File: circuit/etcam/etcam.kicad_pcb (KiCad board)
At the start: 2 copper layers, 100 x 50 mm, 86 parts, among them J1 SWD_connector, J2 USB_connector, J3 ESC_signal_connector, J4 ESC_GND_connector, J5 MCU_PWR_SRC_selector, J6 jumper_park, SW1 reset_SW, U1 FT232RL, U2 Si8640BB-B-IS1, U3 Si8640BB-B-IS1, U4 Si8640BB-B-IS1, U5 Si8640BB-B-IS1, U6 74HC251, U7 STM32F303xD/E-LQFP64, U8 LM1117-3.3, U9 ADuM5020, Y1 8MHz

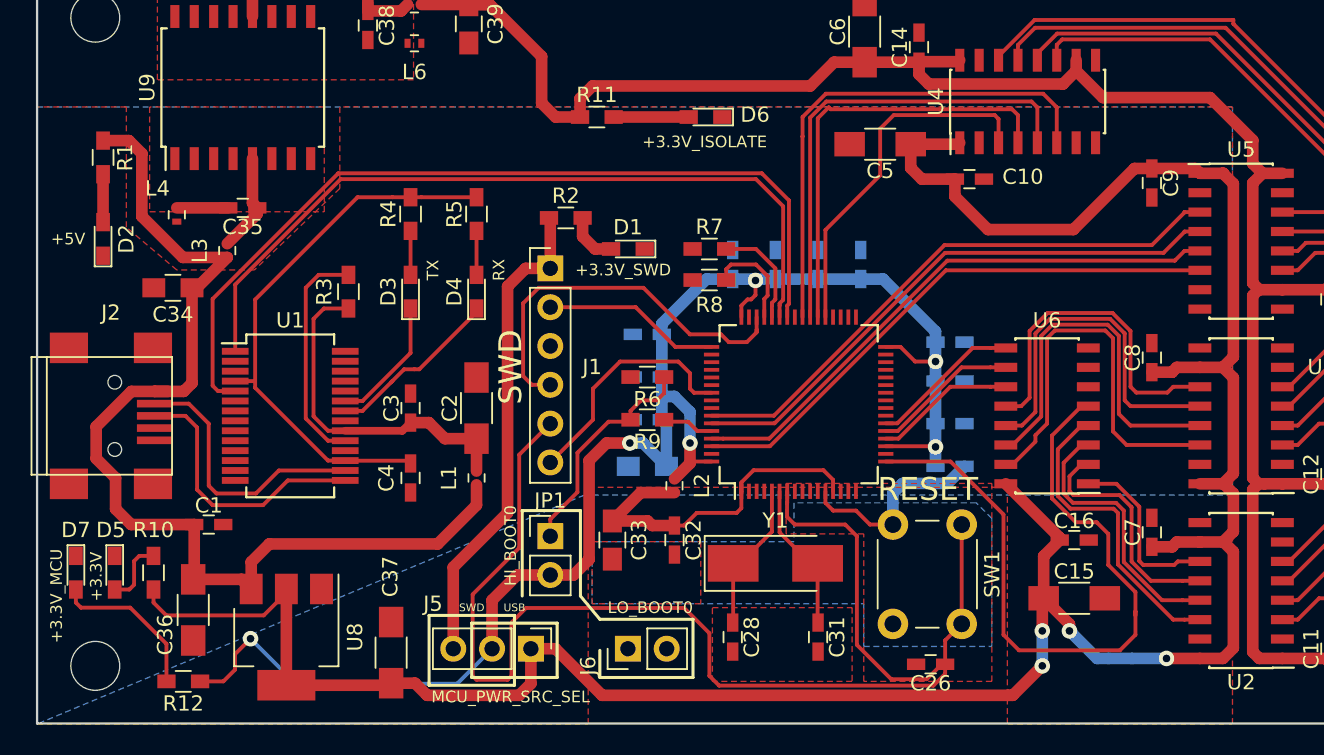
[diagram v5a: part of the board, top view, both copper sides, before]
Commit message: added via between front and back GND plane in ETCAM PCB
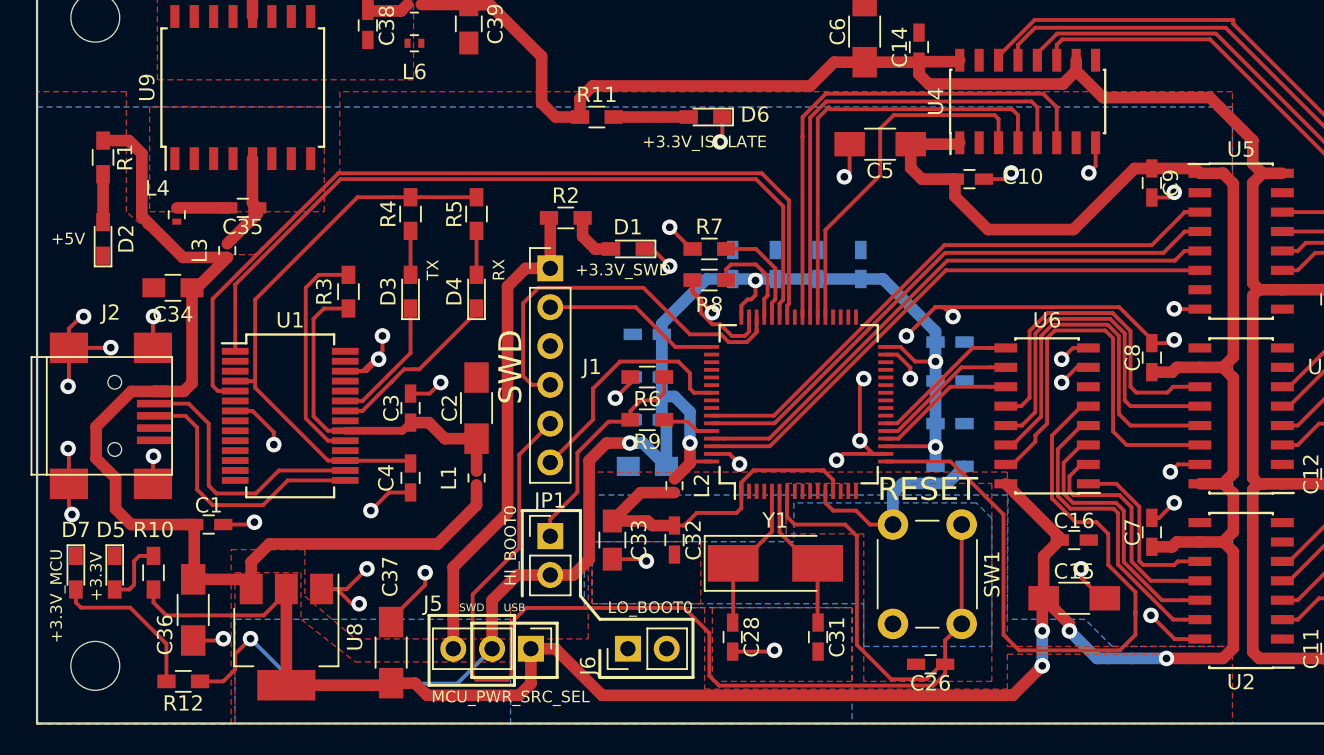
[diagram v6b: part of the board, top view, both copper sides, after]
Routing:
- net GND: track 13.2 -> 142.1 mm, vias 0 -> 43
- added copper zone on F.Cu, net /+3.3V_USB

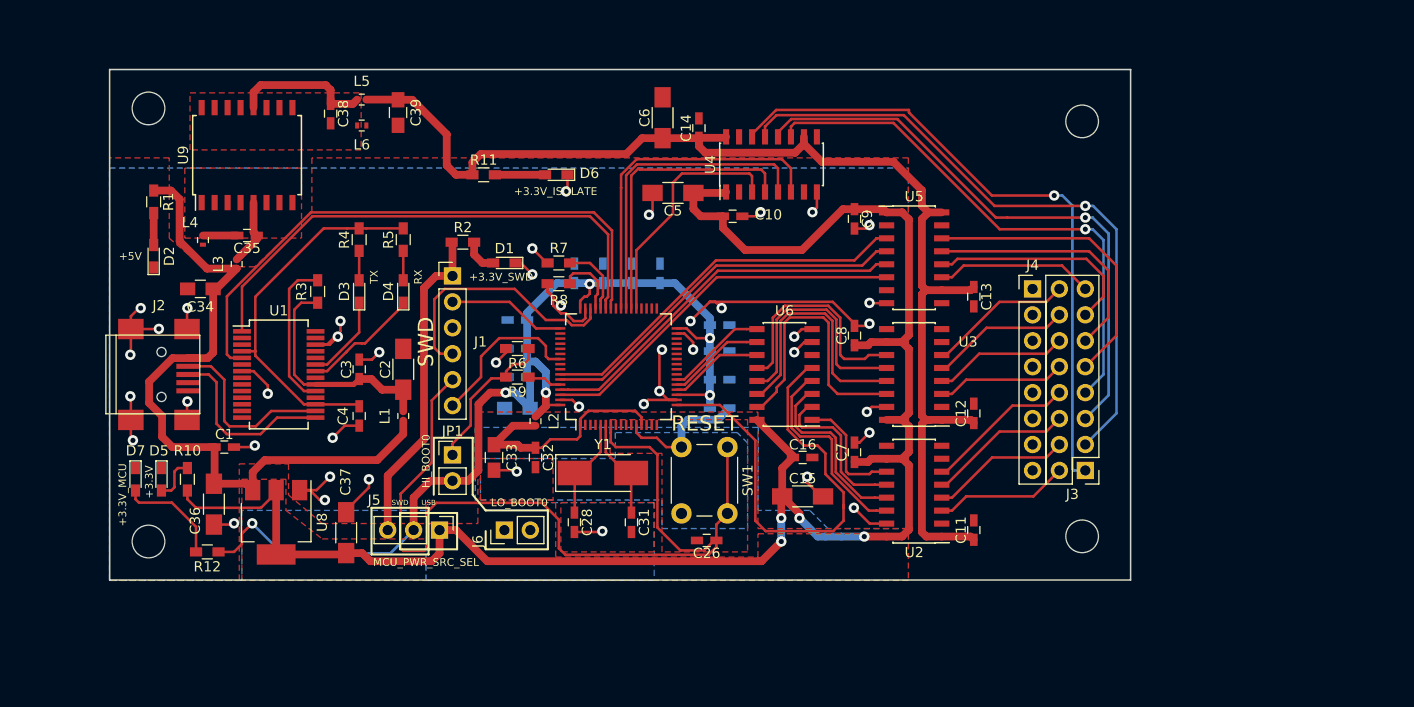
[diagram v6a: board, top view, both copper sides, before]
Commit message: added GNDPWR pland to ETCAM PCB
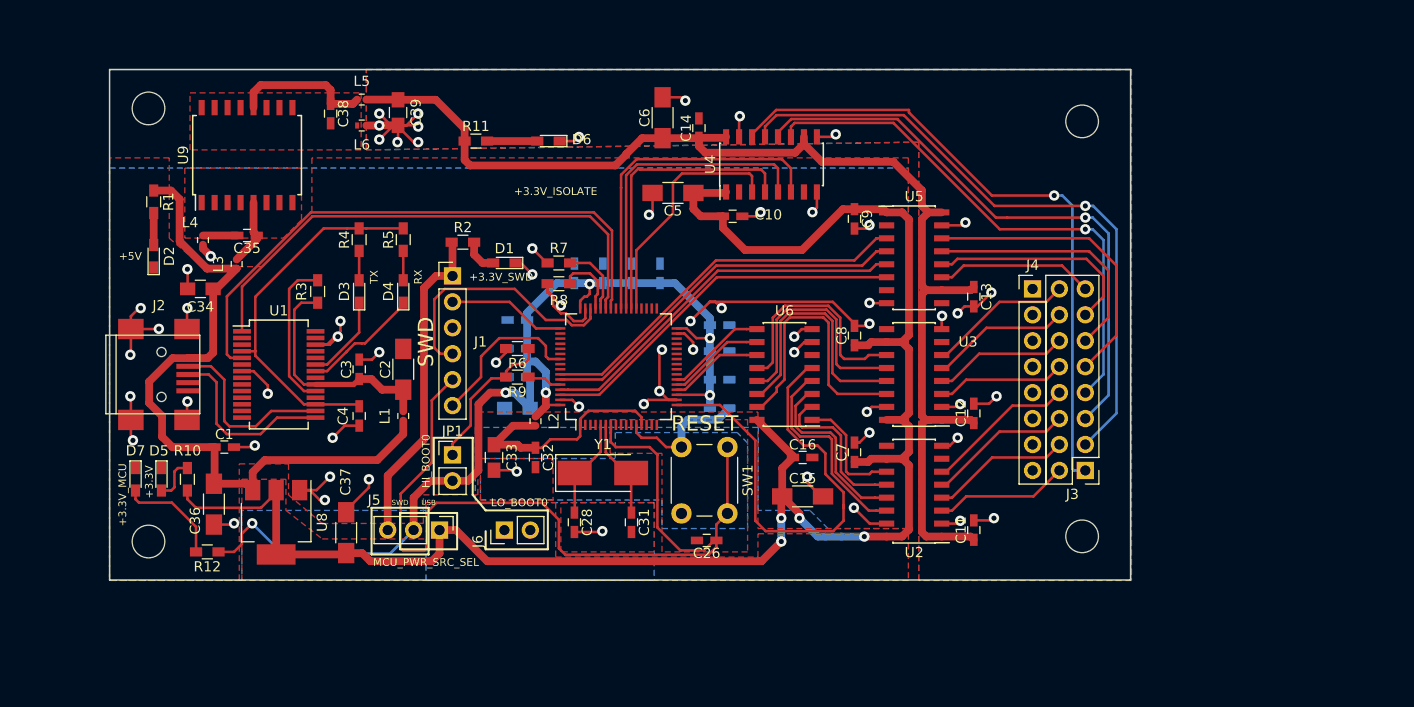
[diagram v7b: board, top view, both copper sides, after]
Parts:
- moved D6 3.39 mm to (135.9, 74.2)
- moved R11 3.39 mm to (128.8, 74.2)
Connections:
- D6 pad 1: GND -> GNDPWR
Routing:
- net GNDPWR: track 0.00 -> 43.4 mm, vias 0 -> 20
- net GND: track 142.1 -> 143.8 mm, vias 43 -> 44
- net /+3.3V_ISOLATOR: track 119.2 -> 117.8 mm
- added copper zone on B.Cu, net GNDPWR
- added copper zone on F.Cu, net GNDPWR

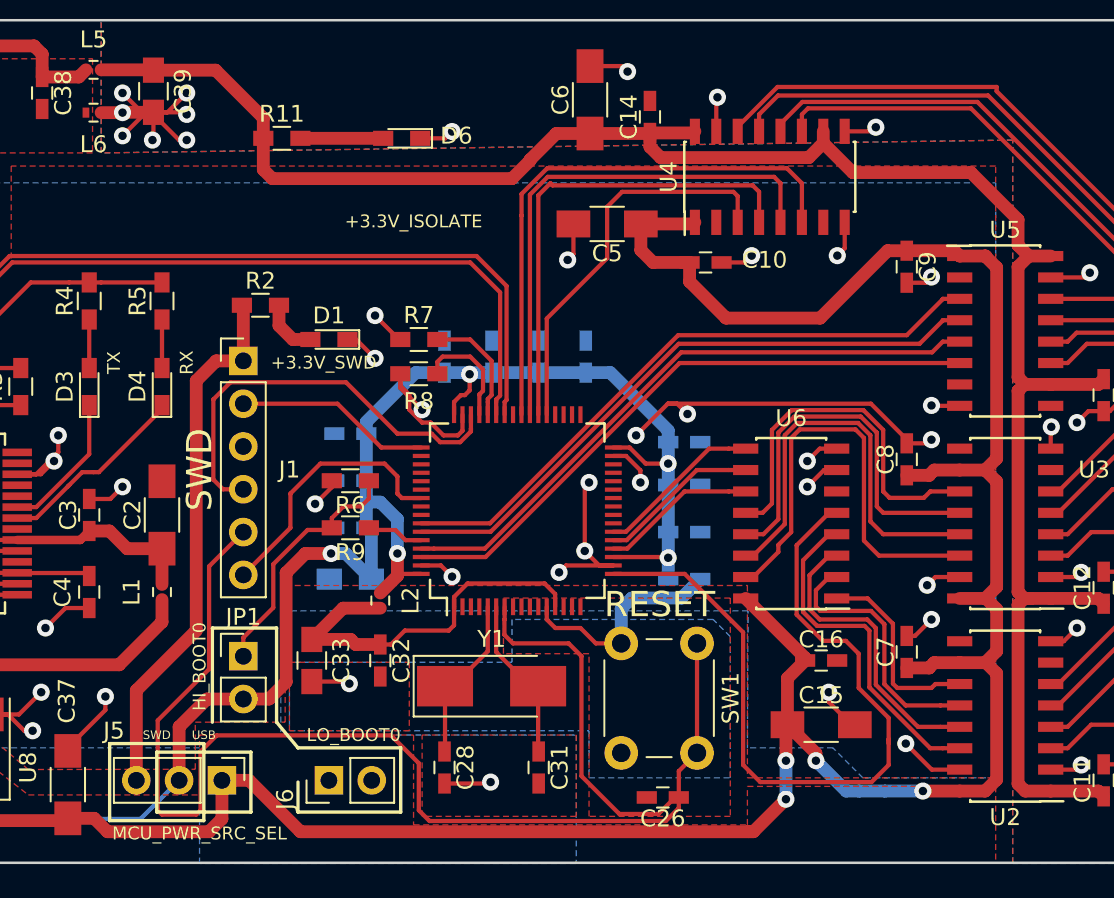
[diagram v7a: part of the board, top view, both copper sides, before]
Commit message: fixed position of 3.3V_ISOLATOR_LED label in ETCAM PCB
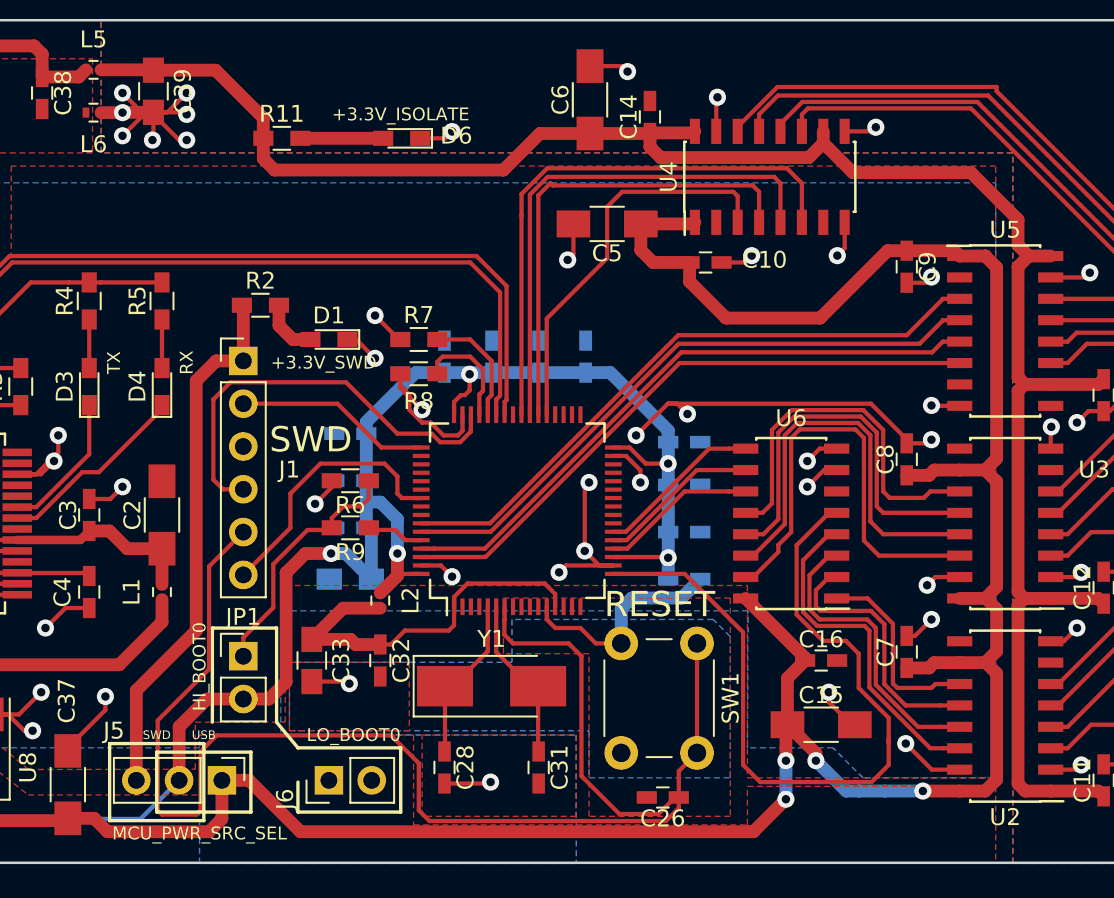
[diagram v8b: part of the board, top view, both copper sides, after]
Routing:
- net /+3.3V_ISOLATOR: track 117.8 -> 116.9 mm
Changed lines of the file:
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@@
     (thickness 1.6)
     (drawings 36)
-    (tracks 906)
+    (tracks 904)
     (zones 0)
     (modules 86)
@@
   )
   (setup
-    (last_trace_width 0.254)
+    (last_trace_width 0.762)
     (user_trace_width 0.508)
     (user_trace_width 0.762)
@@
     (effects (font (size 0.762 0.762) (thickness 0.1905)))
   )
-  (gr_text +3.3V_ISOLATE (at 136.594 79.098) (layer F.SilkS)
+  (gr_text +3.3V_ISOLATE (at 135.832 72.748) (layer F.SilkS)
     (effects (font (size 0.762 0.762) (thickness 0.1905)))
   )
@@
     (effects (font (size 0.762 0.762) (thickness 0.1905)))
   )
-  (gr_text SWD (at 123.894 93.83 90) (layer F.SilkS)
+  (gr_text SWD (at 130.498 92.052 360) (layer F.SilkS)
     (effects (font (size 1.5 1.5) (thickness 0.3)))
   )
@@
   (segment (start 113.074 99.964) (end 117.17 99.964) (width 0.254) (layer F.Cu) (net 5))
   (segment (start 117.17 99.964) (end 117.348 100.142) (width 0.254) (layer F.Cu) (net 5))
+  (segment (start 127.678 74.168) (end 127.678 75.38) (width 0.762) (layer F.Cu) (net 6))
+  (segment (start 127.678 75.38) (end 128.348 76.05) (width 0.762) (layer F.Cu) (net 6))
+  (segment (start 128.348 76.05) (end 141.928 76.05) (width 0.762) (layer F.Cu) (net 6))
+  (segment (start 144.096 73.882) (end 147.066 73.882) (width 0.762) (layer F.Cu) (net 6))
+  (segment (start 141.928 76.05) (end 144.096 73.882) (width 0.762) (layer F.Cu) (net 6))
   (segment (start 121.158 70.124) (end 124.846 70.124) (width 0.762) (layer F.Cu) (net 6))
   (segment (start 124.846 70.124) (end 127.678 72.956) (width 0.762) (layer F.Cu) (net 6))
   (segment (start 127.678 72.956) (end 127.678 74.168) (width 0.762) (layer F.Cu) (net 6))
-  (segment (start 147.066 73.882) (end 145.066 73.882) (width 0.762) (layer F.Cu) (net 6))
-  (segment (start 143.51 75.484) (end 142.436 76.558) (width 0.762) (layer F.Cu) (net 6))
-  (segment (start 127.678 76.024) (end 127.678 74.168) (width 0.762) (layer F.Cu) (net 6))
-  (segment (start 145.066 73.882) (end 143.51 75.438) (width 0.762) (layer F.Cu) (net 6))
-  (segment (start 143.51 75.438) (end 143.51 75.484) (width 0.762) (layer F.Cu) (net 6))
-  (segment (start 142.436 76.558) (end 128.212 76.558) (width 0.762) (layer F.Cu) (net 6))
-  (segment (start 128.212 76.558) (end 127.678 76.024) (width 0.762) (layer F.Cu) (net 6))
   (segment (start 118.052 70.104) (end 121.138 70.104) (width 0.762) (layer F.Cu) (net 6))
   (segment (start 121.138 70.104) (end 121.158 70.124) (width 0.762) (layer F.Cu) (net 6))
@@
       (pts
         (xy 118.052 75.034) (xy 118.052 67.16) (xy 192.982 67.16) (xy 192.982 117.198) (xy 172.154 117.198)
-        (xy 172.154 74.272)
+        (xy 172.154 75.034)
       )
     )
@@
       (pts
         (xy 118.052 75.034) (xy 118.052 67.16) (xy 192.982 67.16) (xy 192.982 117.198) (xy 172.154 117.198)
-        (xy 172.154 74.272)
+        (xy 172.154 75.034)
       )
     )
